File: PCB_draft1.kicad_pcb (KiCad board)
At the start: 2 copper layers, 87 parts, among them J13 RaspPi_Conn, J14 Motor_5_Conn, J15 UART_Bridge_TXRX, J16 Test_Conns, J19 TOF_Connectors, J2 Motor_4_Conn, J21 IMU_Conn, J3 USB_B_Micro, J5 Motor_3_Conn, J6 Motor_2_Conn, J7 5V_Input, J8 Motor_1_Conn, Q5 NMOS, Q6 NMOS, Q7 NMOS, Q8 NMOS, Q9 NMOS, SW1 SW_Push, SW2 SW_Push, U1 AP63203WU, U2 SAM-M8Q, U3 ESP32-S3-WROOM-1

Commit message: pcb layout done, billy watching over us
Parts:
- added G***: LOGO, Graphics:image_silksong, F.Cu at (160.0, 90.0)
- added REF**: MountingHole_3.2mm_M3, MountingHole:MountingHole_3.2mm_M3, F.Cu at (171.0, 32.0)
- added REF**: MountingHole_3.2mm_M3, MountingHole:MountingHole_3.2mm_M3, F.Cu at (31.5, 121.5)
- added REF**: MountingHole_3.2mm_M3, MountingHole:MountingHole_3.2mm_M3, F.Cu at (171.5, 121.0)
- added REF**: MountingHole_3.2mm_M3, MountingHole:MountingHole_3.2mm_M3, F.Cu at (31.0, 56.5)
- added TP1: TestPoint, TestPoint:TestPoint_Pad_D1.5mm, F.Cu at (121.5, 91.0)
- added TP10: TestPoint, TestPoint:TestPoint_Pad_D1.5mm, F.Cu at (115.0, 42.0)
- added TP11: TestPoint, TestPoint:TestPoint_Pad_D1.5mm, F.Cu at (98.5, 42.5)
- added TP12: TestPoint, TestPoint:TestPoint_Pad_D1.5mm, F.Cu at (84.0, 42.5)
- added TP2: TestPoint, TestPoint:TestPoint_Pad_D1.5mm, F.Cu at (74.5, 70.5)
- added TP7: TestPoint, TestPoint:TestPoint_Pad_D1.5mm, F.Cu at (147.5, 44.0)
- added TP8: TestPoint, TestPoint:TestPoint_Pad_D1.5mm, F.Cu at (130.5, 41.5)
- added TP9: TestPoint, TestPoint:TestPoint_Pad_D1.5mm, F.Cu at (50.0, 50.0)
- moved J6 114.4 mm to (100.4, 31.0), turned to 180 degrees
- moved R18 114.2 mm to (95.4, 35.5), turned to 0 degrees
- moved R20 109.7 mm to (79.4, 35.0), turned to 0 degrees
- moved J8 108.9 mm to (84.9, 31.0), turned to 180 degrees
- moved D36 108.4 mm to (126.5, 85.5), turned to 0 degrees
- moved D8 107.8 mm to (99.3, 38.0), turned to 0 degrees
- moved SW1 105.8 mm to (129.5, 94.5), turned to -90 degrees
- moved Q8 104.7 mm to (105.2, 36.0), turned to 0 degrees
- moved C11 104.0 mm to (126.5, 90.0), turned to 180 degrees
- moved D9 103.3 mm to (83.9, 37.0), turned to 0 degrees
- moved R17 101.5 mm to (104.4, 39.5), turned to 0 degrees
- moved Q9 99.2 mm to (89.6, 36.0), turned to 0 degrees
- moved R28 96.6 mm to (71.5, 101.0), turned to 90 degrees
- moved R19 96.0 mm to (88.8, 39.5), turned to 0 degrees
- moved R9 92.5 mm to (76.0, 101.0), turned to 90 degrees
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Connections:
- D4 pad 1: /Motor Drivers/Motor5_In -> /Motor Drivers/Motor_5_in
- D4 pad 2: /Motor Drivers/Motor5_Out -> /Motor Drivers/Motor_5_out
- D5 pad 1: /Motor Drivers/Motor5_In -> /Motor Drivers/Motor_4_in
- D5 pad 2: /Motor Drivers/Motor5_Out -> /Motor Drivers/Motor_4_out
- D7 pad 1: /Motor Drivers/Motor5_In -> /Motor Drivers/Motor_3_in
- D7 pad 2: /Motor Drivers/Motor5_Out -> /Motor Drivers/Motor_3_out
- D8 pad 1: /Motor Drivers/Motor5_In -> /Motor Drivers/Motor_2_in
- D8 pad 2: /Motor Drivers/Motor5_Out -> /Motor Drivers/Motor_2_out
- D9 pad 1: /Motor Drivers/Motor5_In -> /Motor Drivers/Motor_1_in
- D9 pad 2: /Motor Drivers/Motor5_Out -> /Motor Drivers/Motor_1_out
- J14 pad 1: /Motor Drivers/Motor5_Out -> /Motor Drivers/Motor_5_out
- J14 pad 2: /Motor Drivers/Motor5_In -> /Motor Drivers/Motor_5_in
- J2 pad 1: /Motor Drivers/Motor5_Out -> /Motor Drivers/Motor_4_out
- J2 pad 2: /Motor Drivers/Motor5_In -> /Motor Drivers/Motor_4_in
- J3 pad 10: (no net) -> Net-(J3-Shield)
- J3 pad 11: (no net) -> Net-(J3-Shield)
- J3 pad 12: (no net) -> Net-(J3-Shield)
- J3 pad 7: (no net) -> Net-(J3-Shield)
- J3 pad 8: (no net) -> Net-(J3-Shield)
- J3 pad 9: (no net) -> Net-(J3-Shield)
- J5 pad 1: /Motor Drivers/Motor5_Out -> /Motor Drivers/Motor_3_out
- J5 pad 2: /Motor Drivers/Motor5_In -> /Motor Drivers/Motor_3_in
- J6 pad 1: /Motor Drivers/Motor5_Out -> /Motor Drivers/Motor_2_out
- J6 pad 2: /Motor Drivers/Motor5_In -> /Motor Drivers/Motor_2_in
- J8 pad 1: /Motor Drivers/Motor5_Out -> /Motor Drivers/Motor_1_out
- J8 pad 2: /Motor Drivers/Motor5_In -> /Motor Drivers/Motor_1_in
- Q5 pad 1: /Motor Drivers/Motor5_Out -> /Motor Drivers/Motor_5_out
- Q6 pad 1: /Motor Drivers/Motor5_Out -> /Motor Drivers/Motor_4_out
- Q7 pad 1: /Motor Drivers/Motor5_Out -> /Motor Drivers/Motor_3_out
- Q8 pad 1: /Motor Drivers/Motor5_Out -> /Motor Drivers/Motor_2_out
- Q9 pad 1: /Motor Drivers/Motor5_Out -> /Motor Drivers/Motor_1_out
- R12 pad 2: /Motor Drivers/Motor5_In -> /Motor Drivers/Motor_4_in
- R16 pad 2: /Motor Drivers/Motor5_In -> /Motor Drivers/Motor_3_in
- R18 pad 2: /Motor Drivers/Motor5_In -> /Motor Drivers/Motor_2_in
- R20 pad 2: /Motor Drivers/Motor5_In -> /Motor Drivers/Motor_1_in
- R8 pad 2: /Motor Drivers/Motor5_In -> /Motor Drivers/Motor_5_in
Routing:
- net GPIO15: track 2.02 -> 89.3 mm, vias 0 -> 2
- net GPIO40: track 5.53 -> 88.2 mm, vias 0 -> 2
- net GPIO16: track 2.03 -> 76.1 mm
- net GPIO39: track 7.29 -> 79.6 mm, vias 0 -> 2
- net /ESP32/GPIO21: track 28.8 -> 100.3 mm
- net GPIO37: track 5.60 -> 77.1 mm, vias 0 -> 2
- net /ESP32/GPIO48: track 27.6 -> 98.5 mm, vias 2 -> 4
- net /ESP32/GPIO47: track 28.5 -> 98.5 mm
- net GND: track 146.8 -> 207.4 mm, vias 4 -> 21
- net GPIO35: track 5.60 -> 65.7 mm, vias 0 -> 2
- net GPIO36: track 6.04 -> 62.6 mm, vias 0 -> 2
- net GPIO9: track 0.00 -> 53.8 mm, vias 0 -> 2
- net GPIO8: track 0.00 -> 52.4 mm, vias 0 -> 2
- net /ESP32/GPIO7: track 23.1 -> 72.5 mm, vias 4 -> 3
- net /ESP32/GPIO6: track 25.6 -> 73.0 mm
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- added copper zone on F.Cu, net +5V
- added copper zone on B.Cu, net GND
- added copper zone on F.Cu, net VCC_3V3
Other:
- board outline added: 152.4 x 101.6 mm
- board text added: "########## ## BOOT ## ##########"
- board text added: "########### ## RESET ## ###########"
- board text added: "5V to 3V3 Power Supply"
- board text added: "NAME: Pathfinder PCB ID: 01 PCB REVISION: 01 DATE: 2026-02-15 AUTHORS: Jackson Dees, Billy Ilkanic, Conner Martin, Neal Singh"

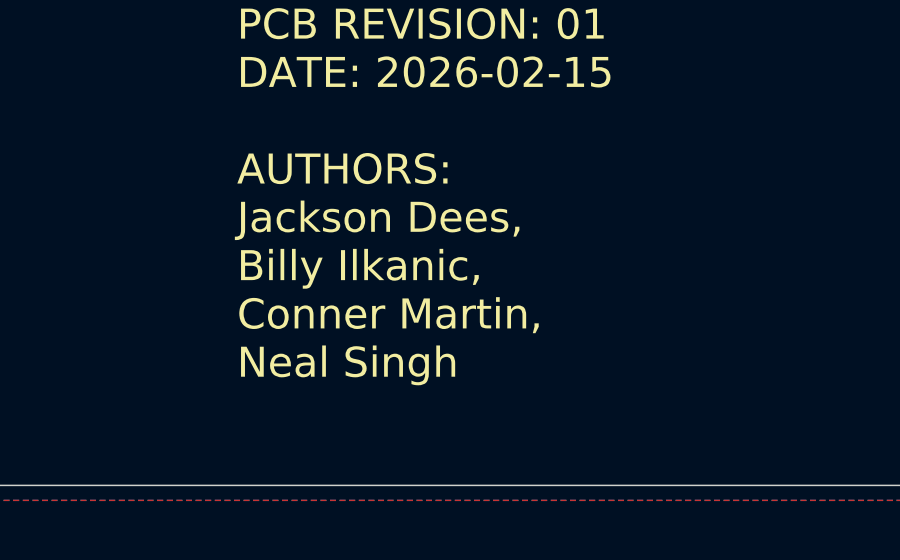
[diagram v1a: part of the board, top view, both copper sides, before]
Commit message: preparing for draft 2 with extra esd protection
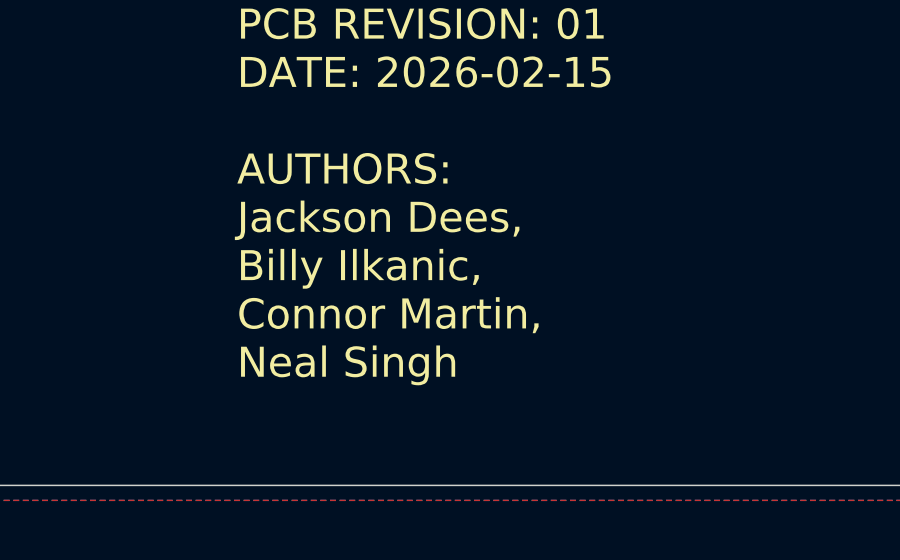
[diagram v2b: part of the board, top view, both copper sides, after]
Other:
- board text added: "NAME: Pathfinder PCB ID: 01 PCB REVISION: 01 DATE: 2026-02-15 AUTHORS: Jackson Dees, Billy Ilkanic, Connor Martin, Neal Singh"
- board text removed: "NAME: Pathfinder PCB ID: 01 PCB REVISION: 01 DATE: 2026-02-15 AUTHORS: Jackson Dees, Billy Ilkanic, Conner Martin, Neal Singh"
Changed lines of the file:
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@@
 		(layer "Edge.Cuts")
 	)
-	(gr_text "NAME: Pathfinder\nPCB ID: 01\nPCB REVISION: 01\nDATE: 2026-02-15\n\nAUTHORS: \nJackson Dees, \nBilly Ilkanic, \nConner Martin, \nNeal Singh"
+	(gr_text "NAME: Pathfinder\nPCB ID: 01\nPCB REVISION: 01\nDATE: 2026-02-15\n\nAUTHORS: \nJackson Dees, \nBilly Ilkanic, \nConnor Martin, \nNeal Singh"
 		(at 147.5 123.5 0)
 		(layer "F.SilkS")

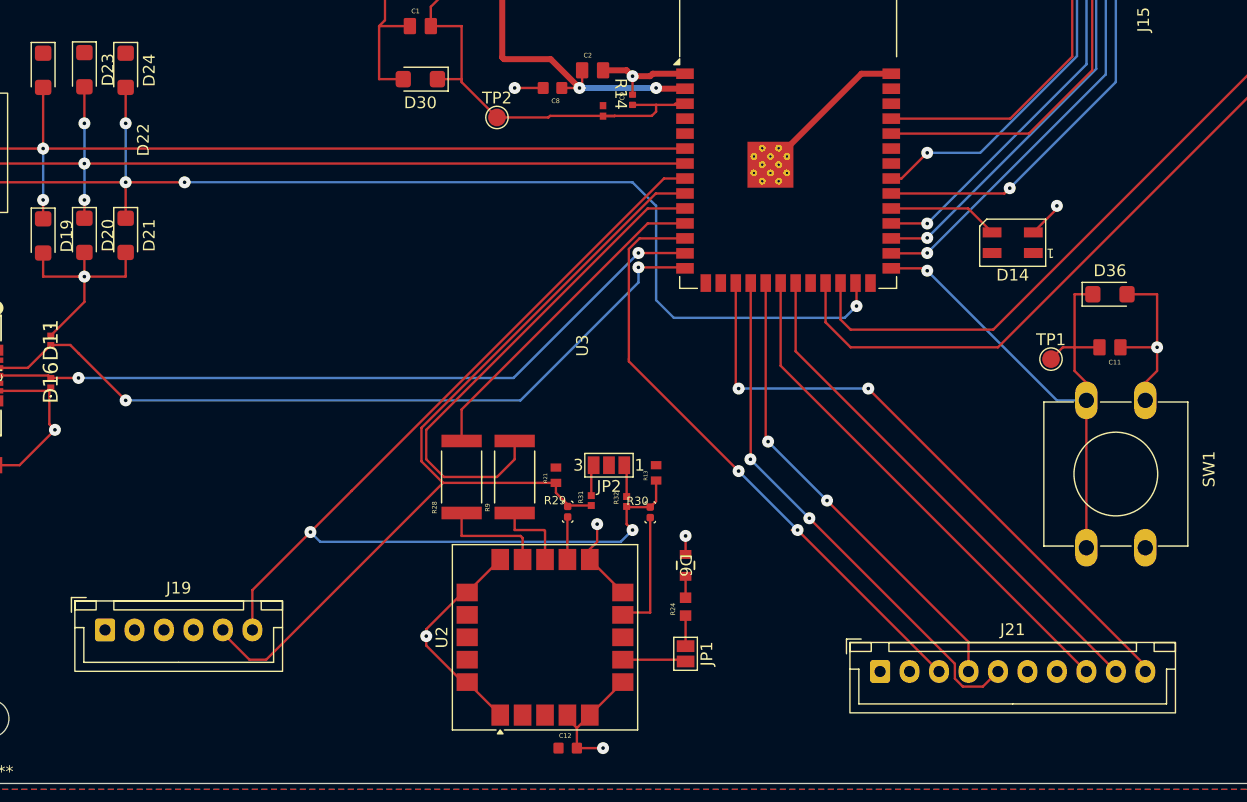
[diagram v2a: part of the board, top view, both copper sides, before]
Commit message: added esd to imu and tof
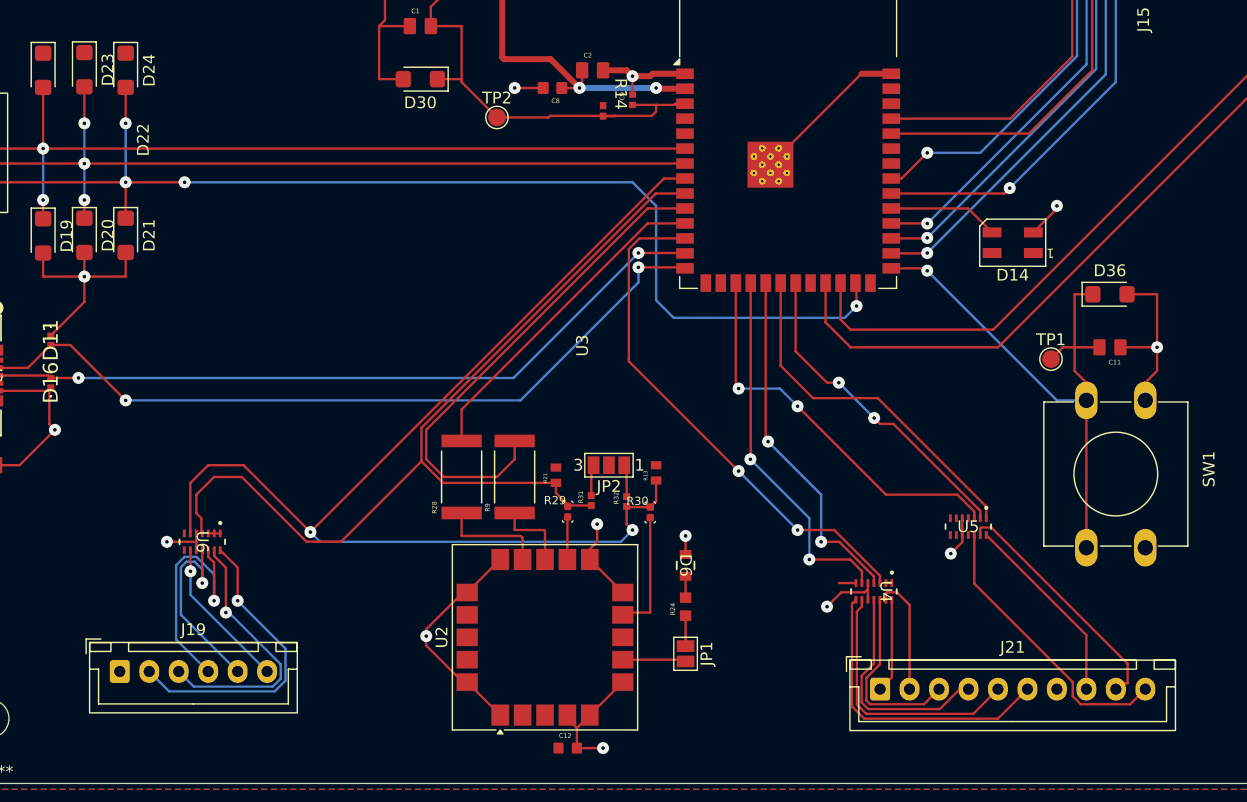
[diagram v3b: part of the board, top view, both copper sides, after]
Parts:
- added U4: SP3011-06UTG, LocalComponents:SON14_SP3011-06UTG_LTF, F.Cu at (106.5, 110.7)
- added U5: SP3011-06UTG, LocalComponents:SON14_SP3011-06UTG_LTF, F.Cu at (114.5, 105.2)
- added U6: SP3011-06UTG, LocalComponents:SON14_SP3011-06UTG_LTF, F.Cu at (49.5, 106.5)
- moved J19 3.74 mm to (42.5, 117.5)
- moved J21 1.50 mm to (107.0, 119.0)
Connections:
- J19 pad 2: VCC_3V3 -> /Peripheral_Sensors/TOF_IOVDD
- J19 pad 3: VCC_3V3 -> /Peripheral_Sensors/TOF_AVDD
- J19 pad 4: VCC_3V3 -> /Peripheral_Sensors/TOF_LPn
- J19 pad 5: GPIO16 -> /Peripheral_Sensors/TOF_SCL
- J19 pad 6: GPIO15 -> /Peripheral_Sensors/TOF_SDA
- J21 pad 1: VCC_3V3 -> Net-(J21-Pin_1)
- J21 pad 10: GPIO9 -> Net-(J21-Pin_10)
- J21 pad 2: VCC_3V3 -> Net-(J21-Pin_2)
- J21 pad 3: GPIO8 -> Net-(J21-Pin_3)
- J21 pad 4: GPIO11 -> Net-(J21-Pin_4)
- J21 pad 5: GPIO10 -> Net-(J21-Pin_5)
- J21 pad 6: VCC_3V3 -> Net-(J21-Pin_6)
- J21 pad 8: GPIO12 -> Net-(J21-Pin_8)
- J21 pad 9: GPIO13 -> Net-(J21-Pin_9)
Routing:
- net /Peripheral_Sensors/TOF_IOVDD: track 0.00 -> 26.0 mm, vias 0 -> 1
- net Net-(J21-Pin_6): track 0.00 -> 25.5 mm
- net Net-(J21-Pin_10): track 0.00 -> 24.1 mm
- net /Peripheral_Sensors/TOF_AVDD: track 0.00 -> 22.8 mm, vias 0 -> 1
- net Net-(J21-Pin_5): track 0.00 -> 22.2 mm
- net /Peripheral_Sensors/TOF_LPn: track 0.00 -> 21.0 mm, vias 0 -> 1
- net Net-(J21-Pin_9): track 0.00 -> 20.7 mm
- net GPIO9: track 53.8 -> 33.9 mm
- net Net-(J21-Pin_4): track 0.00 -> 19.7 mm
- net /Peripheral_Sensors/TOF_SCL: track 0.00 -> 17.1 mm, vias 0 -> 1
- net Net-(J21-Pin_8): track 0.00 -> 16.6 mm
- net GPIO13: track 44.2 -> 27.7 mm, vias 0 -> 2
- net Net-(J21-Pin_3): track 0.00 -> 15.8 mm
- net GPIO10: track 45.4 -> 31.6 mm
- net GPIO12: track 43.7 -> 30.4 mm
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
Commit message: pcb draft 2 from billy
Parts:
- removed G***: LOGO, Graphics:image_silksong
- removed REF** (x4): MountingHole_3.2mm_M3, MountingHole:MountingHole_3.2mm_M3
- removed U6: SP3011-06UTG, LocalComponents:SON14_SP3011-06UTG_LTF
- added D1: ESDS304, Package_TO_SOT_SMD:SOT-23-5, F.Cu at (146.1, 83.0)
- added D2: ESDS304, Package_TO_SOT_SMD:SOT-23-5, F.Cu at (115.8, 83.1)
- D35, D37, D6: footprint LocalComponents:LED_LTST-C171_LTO -> LED_SMD:LED_0201_0603Metric
- L1: value 3.3 uH -> 3.9 uH
- R10, R11, R12, R14, R15, R16, R17, R18, R19, R20, R8: footprint LocalComponents:STA_RMCF0402_STP -> Resistor_SMD:R_0805_2012Metric_Pad1.20x1.40mm_HandSolder
- R13, R21: footprint LocalComponents:RESC1005X40 -> Resistor_SMD:R_0805_2012Metric_Pad1.20x1.40mm_HandSolder
- R24: footprint LocalComponents:RESC1508X55N -> Resistor_SMD:R_0805_2012Metric_Pad1.20x1.40mm_HandSolder
- R27, R34: footprint LocalComponents:RES_ERJ2RKF5101X -> Resistor_SMD:R_0805_2012Metric_Pad1.20x1.40mm_HandSolder
- R28, R9: footprint LocalComponents:RESC6332X65N -> Resistor_SMD:R_0805_2012Metric_Pad1.20x1.40mm_HandSolder
- R29, R30: footprint LocalComponents:R0402 -> Resistor_SMD:R_0805_2012Metric_Pad1.20x1.40mm_HandSolder
- R31, R32: footprint LocalComponents:RESC1005X35N -> Resistor_SMD:R_0805_2012Metric_Pad1.20x1.40mm_HandSolder
- R35: footprint LocalComponents:RESC2012X60N -> Resistor_SMD:R_0805_2012Metric_Pad1.20x1.40mm_HandSolder
- SW1, SW2: footprint Button_Switch_THT:SW_PUSH-12mm -> LocalComponents:ESB335_PAN
- TP1, TP10, TP11, TP12, TP2, TP7, TP8, TP9: footprint TestPoint:TestPoint_Pad_D1.5mm -> TestPoint:TestPoint_Pad_D1.0mm
- moved R35 139.3 mm to (167.7, 72.7), turned to -90 degrees
- moved J3 134.7 mm to (167.4, 67.6), turned to 90 degrees
- moved D16 134.3 mm to (168.1, 65.7), turned to -90 degrees
- moved D11 130.9 mm to (165.4, 65.7)
- moved J19 80.9 mm to (118.5, 89.6), turned to 180 degrees
- moved R13 75.7 mm to (126.8, 35.6), turned to 180 degrees
- moved R21 75.2 mm to (128.5, 43.8), turned to -90 degrees
- moved C8 65.9 mm to (130.6, 26.8)
- moved Q5 65.3 mm to (90.7, 53.8), turned to -90 degrees
- moved R10 64.2 mm to (89.8, 47.7), turned to 90 degrees
- moved TP7 60.6 mm to (87.5, 52.5)
- moved SW2 60.0 mm to (124.7, 64.9), turned to -90 degrees
- moved C2 59.6 mm to (127.2, 27.0), turned to 180 degrees
- moved C9 59.5 mm to (131.5, 30.8), turned to 0 degrees
- moved U3 59.3 mm to (142.8, 31.8)
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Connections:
- net /Motor Drivers/Motor_1_in renamed /Motor Drivers/Motor1_In
- net /Motor Drivers/Motor_1_out renamed /Motor Drivers/Motor1_Out
- net /Motor Drivers/Motor_2_in renamed /Motor Drivers/Motor2_In
- net /Motor Drivers/Motor_2_out renamed /Motor Drivers/Motor2_Out
- net /Motor Drivers/Motor_3_in renamed /Motor Drivers/Motor3_In
- net /Motor Drivers/Motor_3_out renamed /Motor Drivers/Motor3_Out
- net /Motor Drivers/Motor_4_in renamed /Motor Drivers/Motor4_In
- net /Motor Drivers/Motor_4_out renamed /Motor Drivers/Motor4_Out
- net /Motor Drivers/Motor_5_in renamed /Motor Drivers/Motor5_In
- net /Motor Drivers/Motor_5_out renamed /Motor Drivers/Motor5_Out
- J19 pad 2: /Peripheral_Sensors/TOF_IOVDD -> VCC_3V3
- J19 pad 3: /Peripheral_Sensors/TOF_AVDD -> VCC_3V3
- J19 pad 4: /Peripheral_Sensors/TOF_LPn -> VCC_3V3
- J21 pad 1: Net-(J21-Pin_1) -> VCC_3V3
- J21 pad 10: Net-(J21-Pin_10) -> /Peripheral_Sensors/IMU_INT
- J21 pad 2: Net-(J21-Pin_2) -> VCC_3V3
- J21 pad 3: Net-(J21-Pin_3) -> /Peripheral_Sensors/IMU_RST
- J21 pad 4: Net-(J21-Pin_4) -> /Peripheral_Sensors/IMU_DI
- J21 pad 5: Net-(J21-Pin_5) -> /Peripheral_Sensors/IMU_CS
- J21 pad 6: Net-(J21-Pin_6) -> VCC_3V3
- J21 pad 8: Net-(J21-Pin_8) -> /Peripheral_Sensors/IMU_SCL
- J21 pad 9: Net-(J21-Pin_9) -> /Peripheral_Sensors/IMU_SDA
- J3 pad 10: Net-(J3-Shield) -> (no net)
- J3 pad 11: Net-(J3-Shield) -> (no net)
- J3 pad 12: Net-(J3-Shield) -> (no net)
- J3 pad 7: Net-(J3-Shield) -> (no net)
- J3 pad 8: Net-(J3-Shield) -> (no net)
- J3 pad 9: Net-(J3-Shield) -> (no net)
- U4 pad 1: VCC_3V3 -> GPIO8
- U4 pad 11: Net-(J21-Pin_4) -> /Peripheral_Sensors/IMU_SCL
- U4 pad 12: Net-(J21-Pin_3) -> /Peripheral_Sensors/IMU_CS
- U4 pad 13: Net-(J21-Pin_2) -> /Peripheral_Sensors/IMU_DI
- U4 pad 14: Net-(J21-Pin_1) -> /Peripheral_Sensors/IMU_RST
- U4 pad 2: VCC_3V3 -> GPIO11
- U4 pad 3: GPIO8 -> GPIO10
- U4 pad 4: GPIO11 -> GPIO12
- U4 pad 5: GND -> unconnected-(U4-Pad5)
- U4 pad 6: GPIO10 -> GPIO13
- U4 pad 7: VCC_3V3 -> GPIO9
- U4 pad 8: Net-(J21-Pin_6) -> /Peripheral_Sensors/IMU_INT
- U4 pad 9: Net-(J21-Pin_5) -> /Peripheral_Sensors/IMU_SDA
- U5 pad 1: GPIO12 -> GPIO16
- U5 pad 12: Net-(J21-Pin_10) -> unconnected-(U5-Pad12)
- U5 pad 13: Net-(J21-Pin_9) -> /Peripheral_Sensors/TOF_SDA
- U5 pad 14: Net-(J21-Pin_8) -> /Peripheral_Sensors/TOF_SCL
- U5 pad 2: GPIO13 -> GPIO15
- U5 pad 3: GPIO9 -> unconnected-(U5-Pad3)
- U5 pad 5: GND -> unconnected-(U5-Pad5)
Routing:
- net GND: track 220.2 -> 89.9 mm, vias 24 -> 43
- net VCC_3V3: track 102.5 -> 170.4 mm, vias 3 -> 6
- net /ESP32/GPIO21: track 100.3 -> 42.2 mm, vias 2 -> 0
- net /ESP32/GPIO47: track 98.5 -> 43.2 mm, vias 2 -> 0
- net GPIO18: track 28.2 -> 68.9 mm, vias 0 -> 2
- net /ESP32/GPIO48: track 98.5 -> 133.1 mm, vias 4 -> 6
- net /ESP32/GPIO7: track 72.5 -> 105.0 mm, vias 3 -> 5
- net /ESP32/GPIO6: track 73.0 -> 104.5 mm, vias 2 -> 4
- net /ESP32/FT232RL_RX: track 54.1 -> 27.0 mm, vias 2 -> 0
- net /ESP32/FT232RL_TX: track 53.5 -> 26.7 mm, vias 2 -> 0
- net /Peripheral_Sensors/TOF_IOVDD: track 26.0 -> 0.00 mm, vias 1 -> 0
- net GPIO17: track 42.5 -> 68.3 mm, vias 0 -> 2
- net Net-(J21-Pin_6): track 25.5 -> 0.00 mm
- net GPIO39: track 79.6 -> 104.6 mm
- net Net-(J21-Pin_10): track 24.1 -> 0.00 mm
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- added copper zone on F.Cu, net GND
- added copper zone on F.Cu, net Net-(U1-SW)
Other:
- board size 152.4 x 101.6 mm -> 127.2 x 76.1 mm
- board text removed: "########## ## BOOT ## ##########"
- board text removed: "########### ## RESET ## ###########"
- board text removed: "5V to 3V3 Power Supply"
- board text removed: "NAME: Pathfinder PCB ID: 01 PCB REVISION: 01 DATE: 2026-02-15 AUTHORS: Jackson Dees, Billy Ilkanic, Connor Martin, Neal Singh"
